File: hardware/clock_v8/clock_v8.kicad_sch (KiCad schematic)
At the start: 151 parts, among them J1 RJ45, J12 Conn_01x06, J2 Conn_01x06_Pin, J4 Conn_01x04_Pin, J5 Conn_01x06_Pin, J6 Conn_01x04_Pin, J7 Conn_01x04_Pin, J8 Conn_01x02, Q10 2N7002, Q9 2N7002, U1 ADA4807-1, U10 STM32F405RGTx, U11 AMS1117-3.3, U12 BA50DD0WHFP-TR, U13 M24C02-RMN, U2 SN74LVC1G14DBV, U3 SN74LVC1G14DBV, U4 ADA4807-1, U5 ADA4807-1, U6 TLV3603DCKR, U7 SN74LVC1G14DBV, U8 TLV3603DCKR, U9 L78L05_SOT89, Y1 AOCJY4A-10.000MHZ-SW, Y2 16MHz

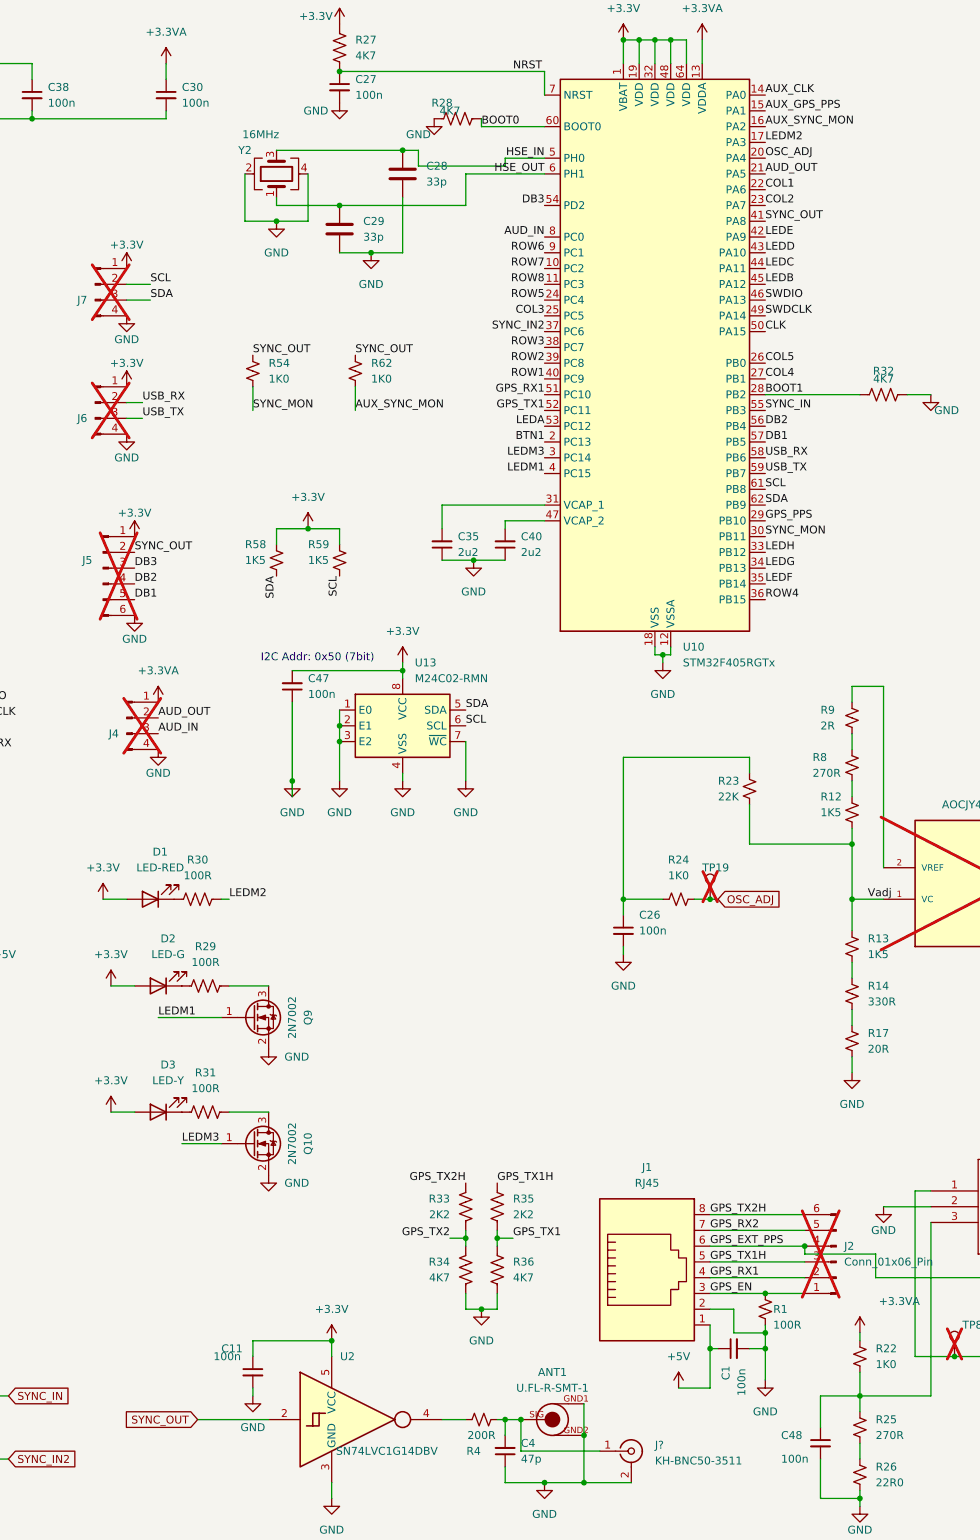
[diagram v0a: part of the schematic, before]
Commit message: rename sync out to pps on v8
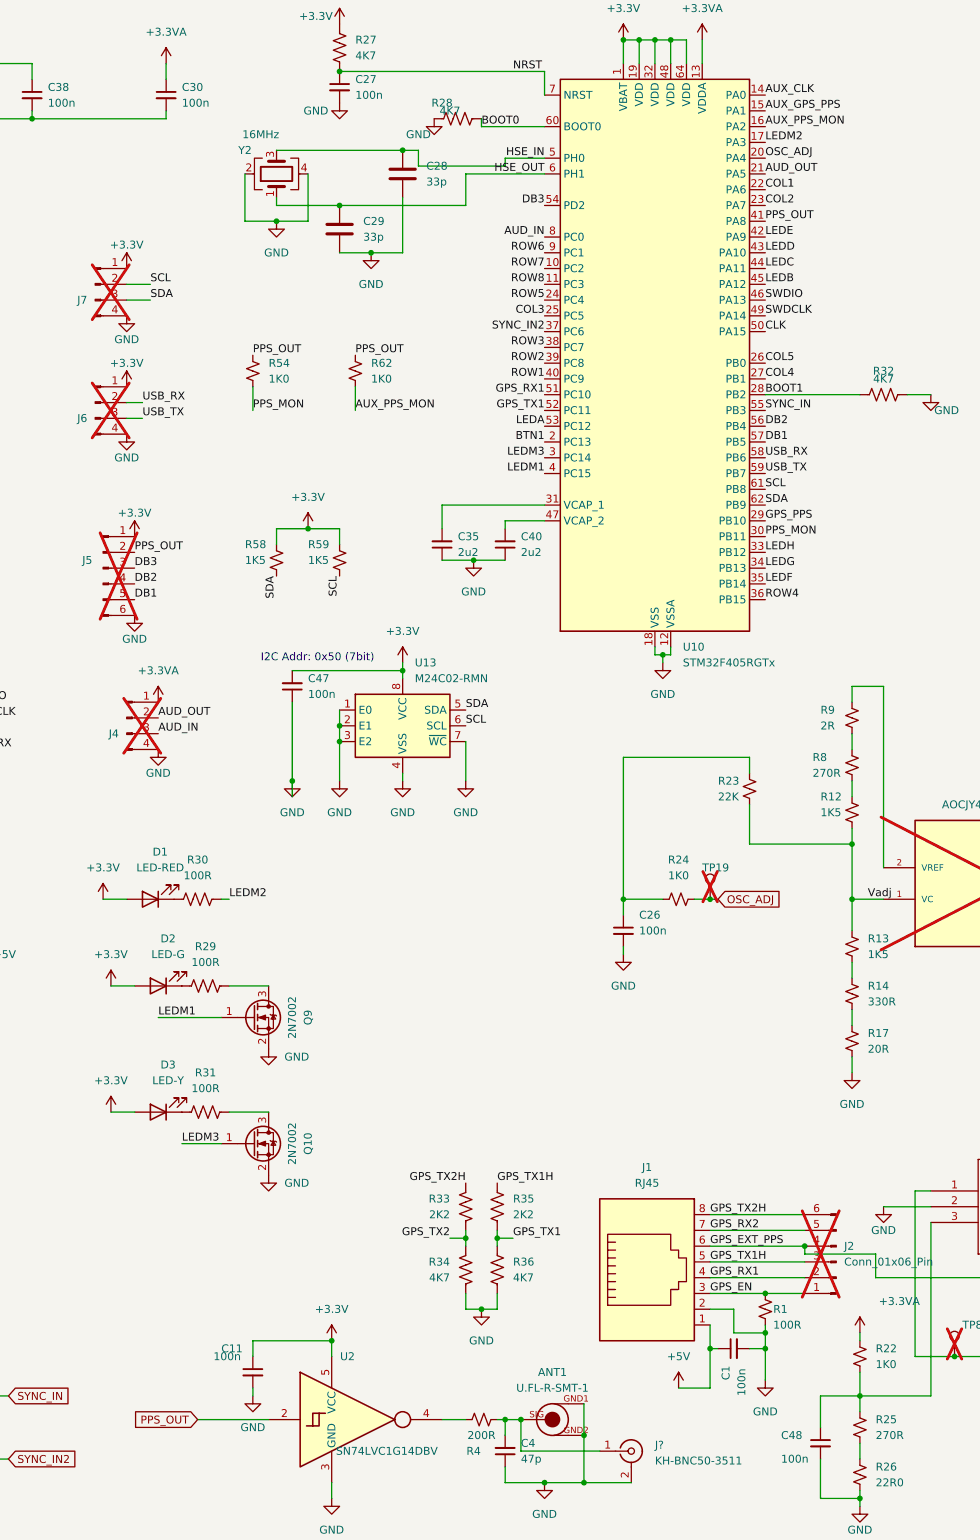
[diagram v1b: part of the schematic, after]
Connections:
- net AUX_SYNC_MON renamed AUX_PPS_MON
- net SYNC_MON renamed PPS_MON
- net SYNC_OUT renamed PPS_OUT
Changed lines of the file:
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@@
     (effects (font (size 1.27 1.27)) (justify left bottom))
   )
-  (label "AUX_SYNC_MON" (at 213.36 38.1 0) (fields_autoplaced)
+  (label "AUX_PPS_MON" (at 213.36 38.1 0) (fields_autoplaced)
     (effects (font (size 1.27 1.27)) (justify left bottom))
   )
@@
     (effects (font (size 1.27 1.27)) (justify left bottom))
   )
-  (label "SYNC_OUT" (at 130.81 74.93 0) (fields_autoplaced)
-    (effects (font (size 1.27 1.27)) (justify left bottom))
-  )
-  (label "SYNC_MON" (at 213.36 104.14 0) (fields_autoplaced)
+  (label "PPS_OUT" (at 130.81 74.93 0) (fields_autoplaced)
+    (effects (font (size 1.27 1.27)) (justify left bottom))
+  )
+  (label "PPS_MON" (at 213.36 104.14 0) (fields_autoplaced)
     (effects (font (size 1.27 1.27)) (justify left bottom))
   )
@@
     (effects (font (size 1.27 1.27)) (justify right bottom))
   )
-  (label "SYNC_OUT" (at 147.32 74.93 0) (fields_autoplaced)
-    (effects (font (size 1.27 1.27)) (justify left bottom))
-  )
-  (label "SYNC_OUT" (at 213.36 53.34 0) (fields_autoplaced)
+  (label "PPS_OUT" (at 147.32 74.93 0) (fields_autoplaced)
+    (effects (font (size 1.27 1.27)) (justify left bottom))
+  )
+  (label "PPS_OUT" (at 213.36 53.34 0) (fields_autoplaced)
     (effects (font (size 1.27 1.27)) (justify left bottom))
   )
@@
     (effects (font (size 1.27 1.27)) (justify left bottom))
   )
-  (label "SYNC_MON" (at 130.81 83.82 0) (fields_autoplaced)
-    (effects (font (size 1.27 1.27)) (justify left bottom))
-  )
-  (label "AUX_SYNC_MON" (at 147.32 83.82 0) (fields_autoplaced)
+  (label "PPS_MON" (at 130.81 83.82 0) (fields_autoplaced)
+    (effects (font (size 1.27 1.27)) (justify left bottom))
+  )
+  (label "AUX_PPS_MON" (at 147.32 83.82 0) (fields_autoplaced)
     (effects (font (size 1.27 1.27)) (justify left bottom))
   )
@@
     (effects (font (size 1.27 1.27)) (justify right bottom))
   )
-  (label "SYNC_OUT" (at 111.76 106.68 0) (fields_autoplaced)
+  (label "PPS_OUT" (at 111.76 106.68 0) (fields_autoplaced)
     (effects (font (size 1.27 1.27)) (justify left bottom))
   )
@@
     )
   )
-  (global_label "SYNC_OUT" (shape input) (at 121.92 246.38 180) (fields_autoplaced)
+  (global_label "PPS_OUT" (shape input) (at 121.92 246.38 180) (fields_autoplaced)
     (effects (font (size 1.27 1.27)) (justify right))
     (property "Intersheetrefs" "${INTERSHEET_REFS}" (at 109.5194 246.38 0)

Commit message: start mapping v8 clock pins to match bliky
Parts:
- removed ANT3, ANT4, ANT5: U.FL-R-SMT-1, blinky_footprints:U.FL-R-SMT-1, symbol blinky:U.FL-R-SMT-1
- removed H1, H2, H3, H4, H5: M2, MountingHole:MountingHole_2.2mm_M2, symbol Mechanical:MountingHole
- removed J4, J7: Conn_01x04_Pin, Connector_PinHeader_2.54mm:PinHeader_1x04_P2.54mm_Vertical, symbol Connector:Conn_01x04_Pin
- removed TP8, TP9: ~, TestPoint:TestPoint_THTPad_D1.5mm_Drill0.7mm, symbol Connector:TestPoint
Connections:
- net LEDM1 is gone; now on net NCOL1: Q9.1 (G), U10.4 (PC15)
- net COL1 renamed LED1
- net COL2 renamed LED2
- net COL3 renamed LED8
- net COL4 renamed LED10
- net COL5 renamed LED9
- net DB1 renamed NROW5
- net DB2 renamed LED3
- net LEDA renamed NCOL9
- net LEDB renamed LEDMR
- net LEDC renamed LEDMG
- net LEDD renamed LEDMY
- net LEDE renamed NCOL1
- net LEDF renamed NCOL6
- net LEDG renamed NCOL7
- net LEDH renamed NCOL8
- net LEDM2 renamed LED4
- net LEDM3 renamed NCOL10
- net ROW1 renamed NCOL2
- net ROW2 renamed NCOL3
- net ROW3 renamed NCOL4
- net ROW4 renamed NCOL5
- net ROW5 renamed LED7
- net ROW6 renamed NROW2
- net ROW7 renamed NROW3
- net ROW8 renamed NROW4
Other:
- note removed: "Mounting Holes"

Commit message: clean up clock 8 to match new pinouts
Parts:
- removed ANT1, ANT2: U.FL-R-SMT-1, blinky_footprints:U.FL-R-SMT-1, symbol blinky:U.FL-R-SMT-1
- removed TP16, TP17: ~, TestPoint:TestPoint_THTPad_D1.5mm_Drill0.7mm, symbol Connector:TestPoint
- added Q1: 2N7002, Package_TO_SOT_SMD:SOT-23, symbol Transistor_FET:2N7002
- S1, S2: Comment (none) -> 147873-2; Configuration_Pole-Throw (none) -> Single Pole - Single Throw; Contact_Current_Rating (none) -> 50 mA; JLCPCB Part # (none) -> C266189
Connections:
- net GND: now also Q1.2 (S)
- net LED4: no longer R30.2
- net LEDMG: now also Q9.1 (G)
- net LEDMR: now also Q1.1 (G)
- net LEDMY: now also Q10.1 (G)
- net NCOL1: no longer Q9.1 (G), U10.4 (PC15)
- net NCOL10: no longer Q10.1 (G)
- new net: Q1.3 (D), R30.2
- new net NROW1: U10.4 (PC15)
- no-connect marks 0 -> 24
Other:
- moved on the sheet: C1, C45, C48, D1, D2, D3, J1, J2, J?, Q10, Q9, R1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

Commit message: start add USB to clock
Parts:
- added C50: 100n, Capacitor_SMD:C_0402_1005Metric, symbol Device:C_Small
- added J4: USB_C_Receptacle, Connector_USB:USB_C_Receptacle_HRO_TYPE-C-31-M-12, symbol blinky:USB_C_Receptacle
- added R37, R38: 5k1, Resistor_SMD:R_0402_1005Metric, symbol Device:R
- added S3: 147873-2, SW_147873-2, symbol blinky:147873-2
- added U14: CH340C, Package_SO:SOIC-16_3.9x9.9mm_P1.27mm, symbol Interface_USB:CH340C
- added U15: USBLC6-2P6, Package_TO_SOT_SMD:SOT-666, symbol Power_Protection:USBLC6-2P6
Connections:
- net +3.3V: now also C50.1, S3.2, U14.16 (VCC), U14.4 (V3)
- net BOOT0: now also J5.2 (Pin_2), S3.1
- net BOOT1: now also J5.3 (Pin_3)
- net BTN1: now also J5.4 (Pin_4)
- net DB3: now also J5.5 (Pin_5); no longer J5.3 (Pin_3)
- net GND: now also C50.2, J4.A1 (GND), J4.A12 (GND), J4.B1 (GND), J4.B12 (GND), R37.1, R38.1, U14.1 (GND), U15.2 (GND)
- net LED3: no longer J5.4 (Pin_4)
- net NROW5: no longer J5.5 (Pin_5)
- net PPS_OUT: no longer J5.2 (Pin_2)
- net USB_RX: now also U14.3 (RXD)
- net USB_TX: now also U14.2 (TXD)
- new net: J4.B5 (CC2), R37.2
- new net: J4.A5 (CC1), R38.2
- new net: J4.A6 (D+), J4.B6 (D+), U15.6 (I/O1)
- new net: J4.A7 (D-), J4.B7 (D-), U15.4 (I/O2)
- new net: U14.5 (UD+), U15.1 (I/O1)
- new net: U14.6 (UD-), U15.3 (I/O2)
- new net USB_DTR: U14.13 (~{DTR})
- new net USB_RTS: U14.14 (~{RTS})
- new net VBUS: J4.A4 (VBUS), J4.A9 (VBUS), J4.B4 (VBUS), J4.B9 (VBUS), U15.5 (VBUS)
- no-connect marks 24 -> 32
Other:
- moved on the sheet: C25, C46, C49, R18, R19, R20, TP10, U6, U7

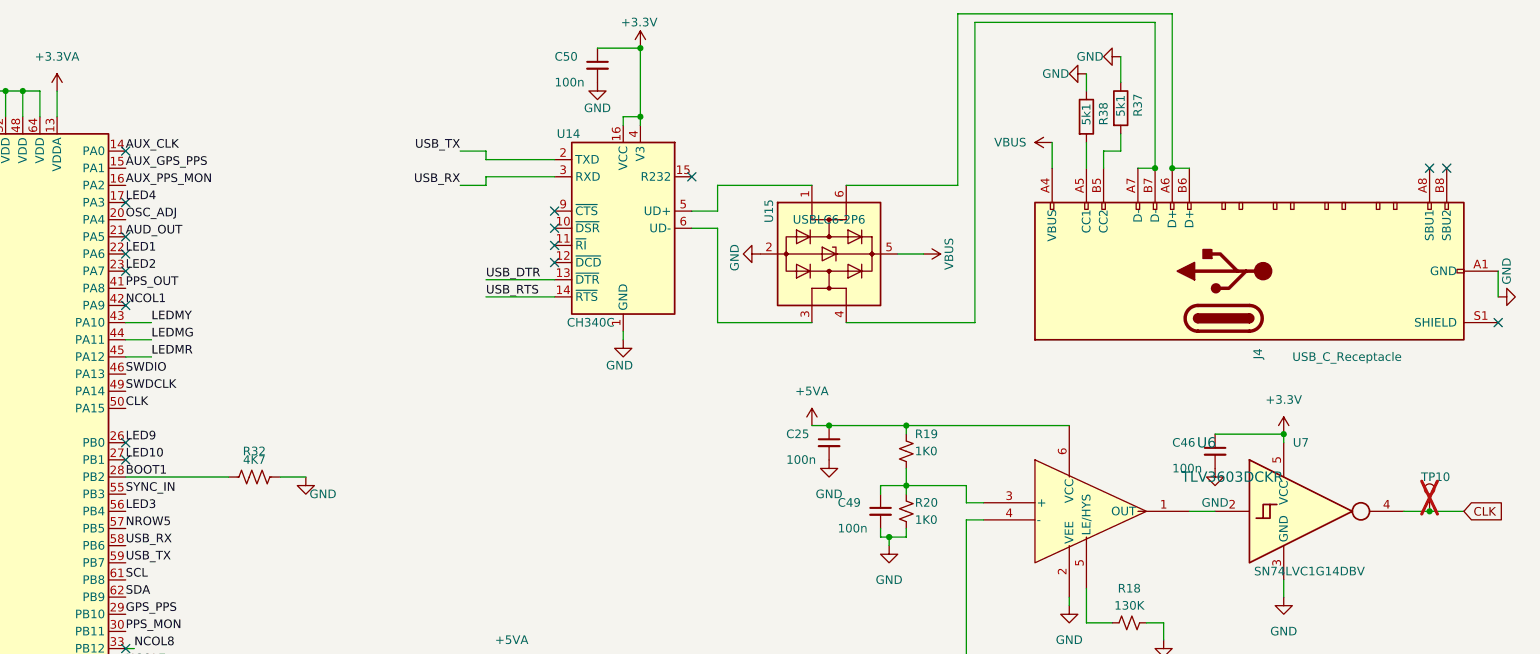
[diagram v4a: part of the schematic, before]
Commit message: move disp to shared sym and footprints
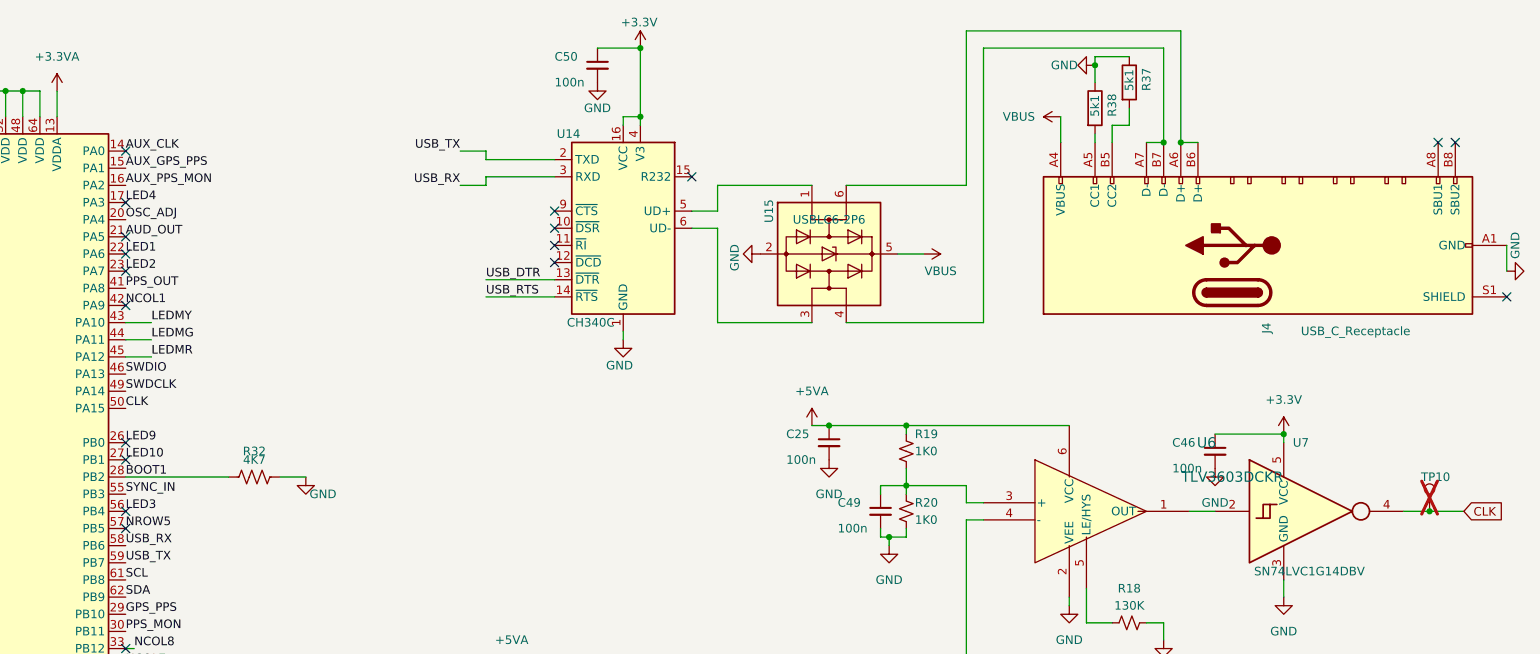
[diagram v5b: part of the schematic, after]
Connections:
- no-connect marks 32 -> 34
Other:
- moved on the sheet: J4, R37, R38
